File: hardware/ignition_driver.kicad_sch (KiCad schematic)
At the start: 12 parts

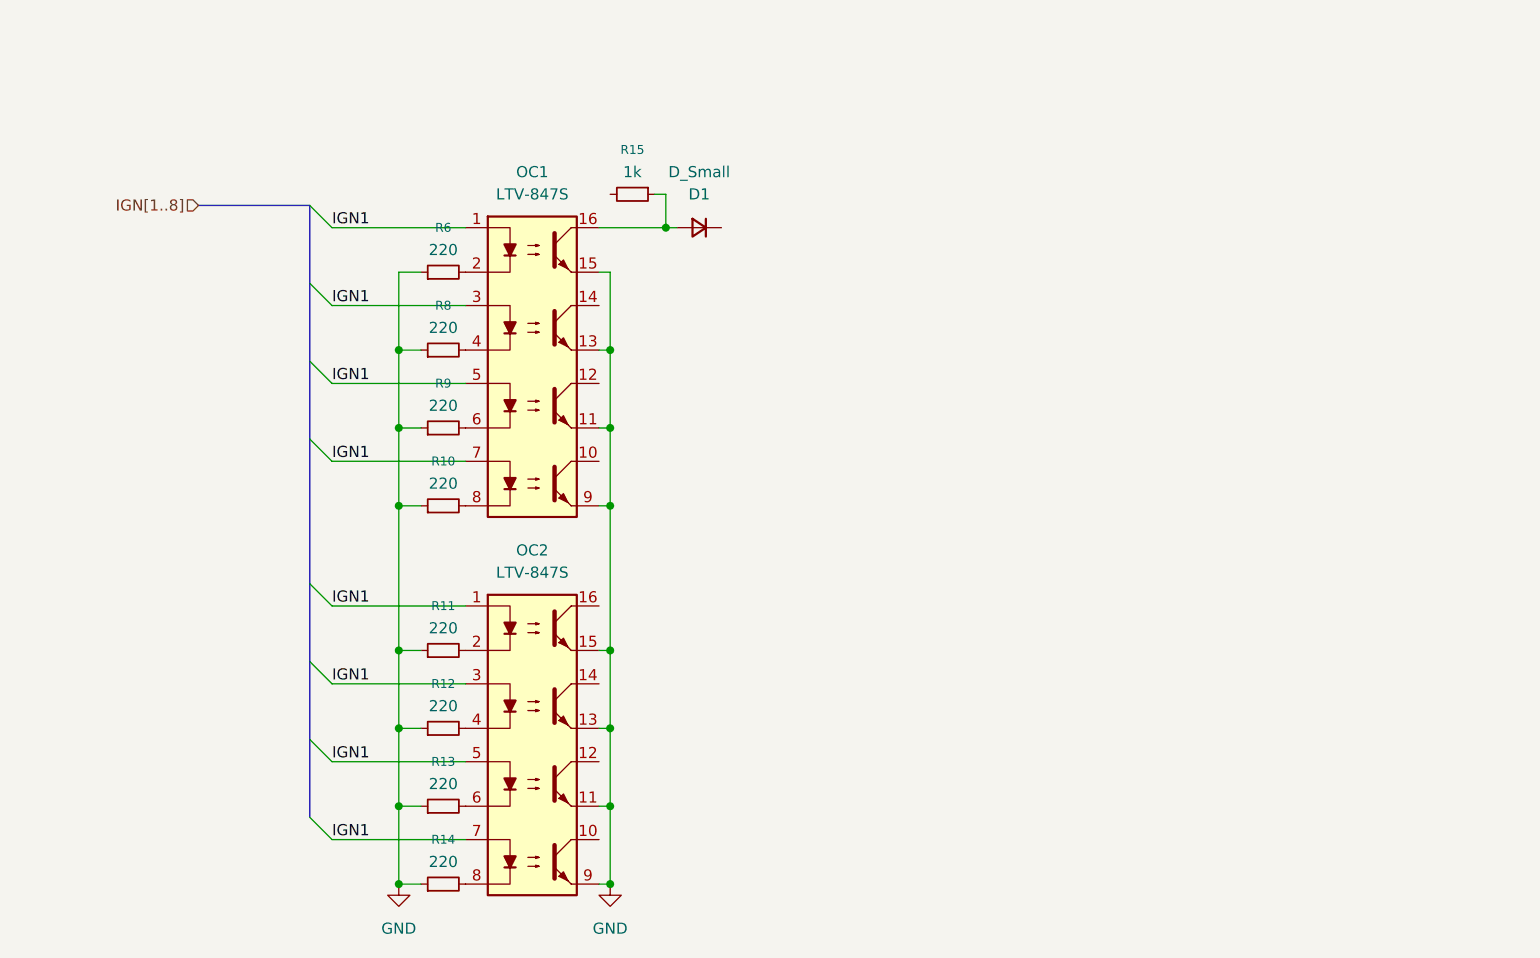
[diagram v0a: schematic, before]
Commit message: Continued IGN driver drawings
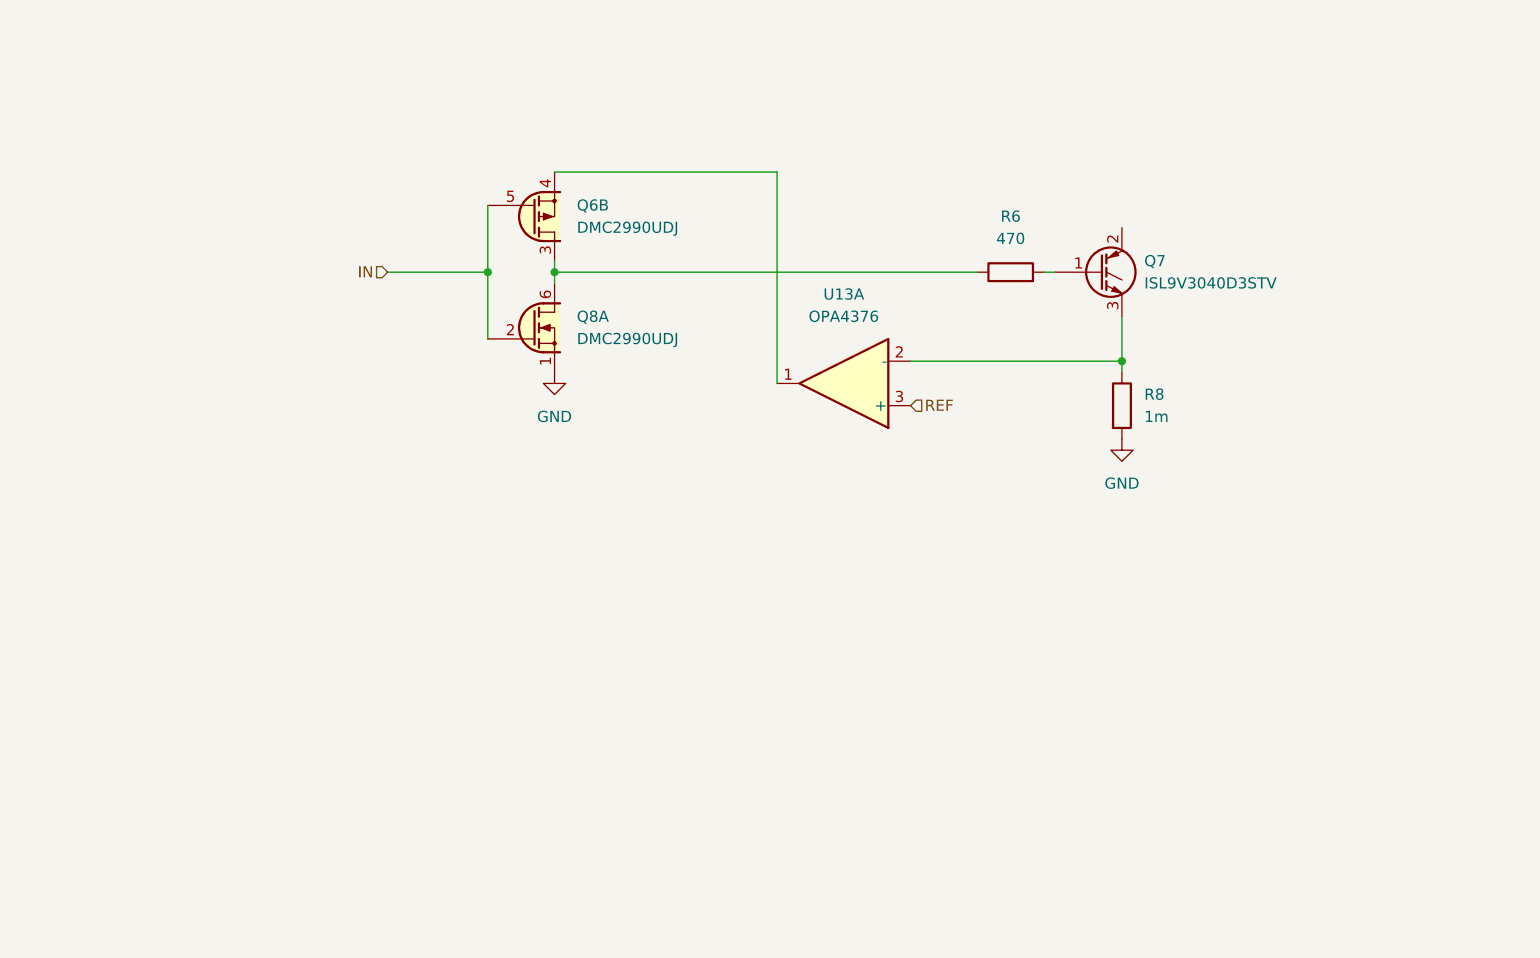
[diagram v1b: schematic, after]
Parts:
- removed D1: D_Small, symbol Device:D_Small
- removed OC1, OC2: LTV-847S, PCM_Package_DIP_AKL:SMDIP-16_W9.53mm, symbol PCM_Optocoupler_AKL:LTV-847S
- removed R10, R11, R12, R13, R14, R6, R8, R9: 220, symbol Device:R_Small
- removed R15: 1k, symbol Device:R_Small
- added Q6, Q8: DMC2990UDJ, PCM_Package_TO_SOT_SMD_AKL:SOT-963, symbol PCM_Transistor_MOSFET_AKL:DMC2990UDJ
- added Q7: ISL9V3040D3STV, Package_TO_SOT_SMD:TO-252-3_TabPin2, symbol Device:Q_NIGBT_GCE
- added R6: 470, symbol Device:R
- added R8: 1m, symbol Device:R
- added U13: OPA4376, symbol Amplifier_Operational:OPA4376
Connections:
- net GND: now also Q8.1 (S1), R8.2
- new net: Q7.1 (G), R6.2
- new net: Q7.3 (E), R8.1, U13.2 (-)
- new net: Q6.4 (S2), U13.1
- new net: Q6.3 (D2), Q8.6 (D1), R6.1
- new net IN: Q6.5 (G2), Q8.2 (G1)
- new net REF: U13.3 (+)

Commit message: Finished preliminary IGN driver
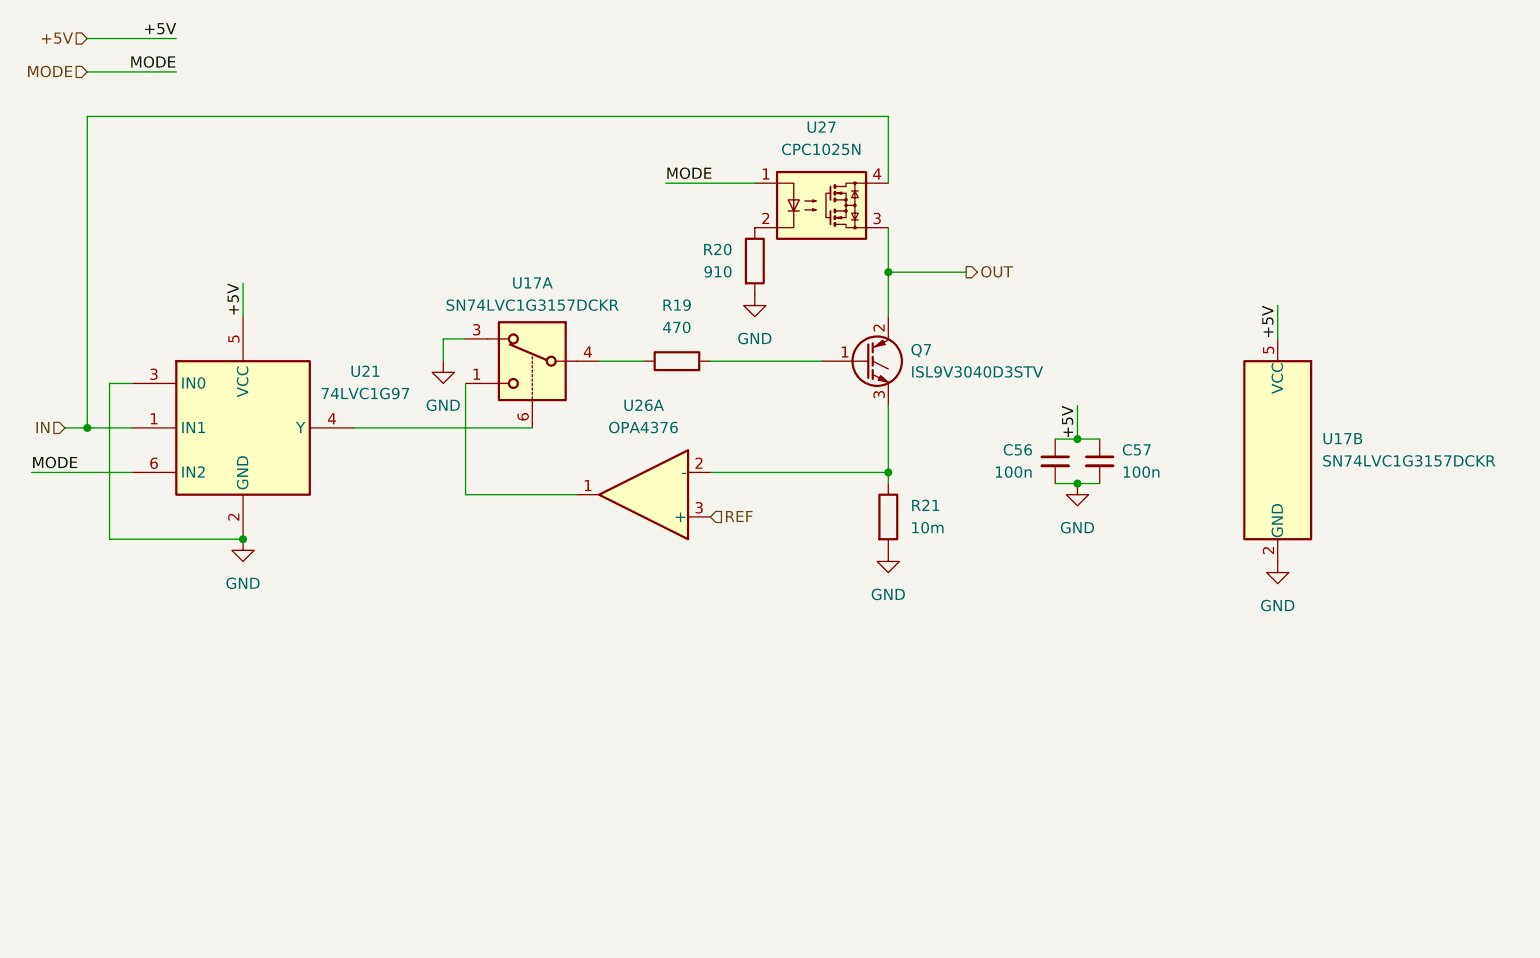
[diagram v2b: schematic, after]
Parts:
- removed Q6, Q8: DMC2990UDJ, PCM_Package_TO_SOT_SMD_AKL:SOT-963, symbol PCM_Transistor_MOSFET_AKL:DMC2990UDJ
- added C56, C57: 100n, symbol Device:C_Small
- added R20: 910, symbol Device:R
- added U17: SN74LVC1G3157DCKR, Package_TO_SOT_SMD:SOT-23-6, symbol openvcu:SN74LVC1G3157DCKR
- added U21: 74LVC1G97, Package_TO_SOT_SMD:SOT-363_SC-70-6, symbol 74xGxx:74LVC1G97
- added U27: CPC1025N, Package_SO:SOP-4_3.8x4.1mm_P2.54mm, symbol Relay_SolidState:CPC1025N
- R21: renamed from R8; value 1m -> 10m
- renumbered R6 to R19, U13 to U26
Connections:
- net GND: now also C56.2, C57.2, R20.2, U17.2 (GND), U17.3, U21.2 (GND), U21.3 (IN0)
- net IN: now also U21.1 (IN1), U27.4
- net OUT: now reaches Q7.2 (C)
- net OUT: now also U27.3
- net at U26.1: now also U17.1
- net at R19.1: now also U17.4
- new net: U17.6, U21.4 (Y)
- new net: R20.1, U27.2
- new net +5V: C56.1, C57.1, U17.5 (VCC), U21.5 (VCC)
- new net MODE: U21.6 (IN2), U27.1
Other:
- moved on the sheet: Q7, R19, R21, U26A

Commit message: Continued work on IGN drivers
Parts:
- removed U26: OPA4376, symbol Amplifier_Operational:OPA4376
- added U13: TSV914, symbol Amplifier_Operational:TSV914
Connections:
- net REF: now also U13.2 (-)
- net at U17.1: now also U13.1
- net at Q7.3 (E), R21.1: now also U13.3 (+)
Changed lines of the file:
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@@
-	)
-	(symbol
-		(lib_id "Amplifier_Operational:OPA4376")
-		(at 92.71 74.93 180)
-		(unit 1)
-		(body_style 1)
-		(exclude_from_sim no)
-		(in_bom yes)
-		(on_board yes)
-		(in_pos_files yes)
-		(dnp no)
-		(fields_autoplaced yes)
-		(property "Reference" "U26"
-			(at 92.71 64.77 0)
-			(show_name no)
-			(do_not_autoplace no)
-			(effects
-				(font
-					(size 1.27 1.27)
-				)
-			)
-		)
-		(property "Value" "OPA4376"
-			(at 92.71 67.31 0)
-			(show_name no)
-			(do_not_autoplace no)
-			(effects
-				(font
-					(size 1.27 1.27)
-				)
-			)
-		)
-		(property "Footprint" ""
-			(at 93.98 77.47 0)
-			(hide yes)
-			(show_name no)
-			(do_not_autoplace no)
-			(effects
-				(font
-					(size 1.27 1.27)
-				)
-			)
-		)
-		(property "Datasheet" "http://www.ti.com/lit/ds/symlink/opa376.pdf"
-			(at 91.44 80.01 0)
-			(hide yes)
-			(show_name no)
-			(do_not_autoplace no)
-			(effects
-				(font
-					(size 1.27 1.27)
-				)
-			)
-		)
-		(property "Description" "Quad Low-Noise, Low Quiescent Current, Precision Operational Amplifier e-trim Series, SC-70-5"
-			(at 92.71 74.93 0)
-			(hide yes)
-			(show_name no)
-			(do_not_autoplace no)
-			(effects
-				(font
-					(size 1.27 1.27)
-				)
-			)
-		)
-		(pin "6"
-		)
-		(pin "5"
-		)
-		(pin "7"
-		)
-		(pin "9"
-		)
-		(pin "14"
-		)
-		(pin "8"
-		)
-		(pin "12"
-		)
-		(pin "1"
-		)
-		(pin "2"
-		)
-		(pin "3"
-		)
-		(pin "10"
-		)
-		(pin "13"
-		)
-		(pin "11"
-		)
-		(pin "4"
-		)
-		(instances
-			(project "openvcu"
-				(path "/474f8017-6a20-4212-a4d1-1038f3d193b2/0e0f3168-a2d1-4cc4-babd-f9e64b91c1ea/6cc00cbf-89c2-4b1d-8fa8-5e3131255cb0"
-					(reference "U26")
-					(unit 1)
-				)
-			)
-		)
 	)
 	(symbol
@@
 					(unit 1)
 				)
+			)
+		)
+	)
+	(symbol
+		(lib_id "Amplifier_Operational:TSV914")
+		(at 92.71 74.93 0)
+		(mirror y)
+		(unit 1)
+		(body_style 1)
+		(exclude_from_sim no)
+		(in_bom yes)
+		(on_board yes)
+		(in_pos_files yes)
+		(dnp no)
+		(property "Reference" "U13"
+			(at 92.71 64.77 0)
+			(show_name no)
+			(do_not_autoplace no)
+			(effects
+				(font
+					(size 1.27 1.27)
+				)
+			)
+		)
+		(property "Value" "TSV914"
+			(at 92.71 67.31 0)
+			(show_name no)
+			(do_not_autoplace no)
+			(effects
+				(font
+					(size 1.27 1.27)
+				)
+			)
+		)
+		(property "Footprint" ""
+			(at 93.98 72.39 0)
+			(hide yes)
+			(show_name no)
+			(do_not_autoplace no)
+			(effects
+				(font
+					(size 1.27 1.27)
+				)
+			)
+		)
+		(property "Datasheet" "www.st.com/resource/en/datasheet/tsv911.pdf"
+			(at 91.44 69.85 0)
+			(hide yes)
+			(show_name no)
+			(do_not_autoplace no)
+			(effects
+				(font
+					(size 1.27 1.27)
+				)
+			)
+		)
+		(property "Description" "Quad rail-to-rail input/output 8 MHz operational amplifiers, SOIC-14/TSSOP-14"
+			(at 92.71 74.93 0)
+			(hide yes)
+			(show_name no)
+			(do_not_autoplace no)
+			(effects
+				(font
+					(size 1.27 1.27)
+				)
+			)
+		)
+		(pin "7"
+		)
+		(pin "13"
+		)
+		(pin "9"
+		)
+		(pin "12"
+		)
+		(pin "3"
+		)
+		(pin "6"
+		)
+		(pin "5"
+		)
+		(pin "10"
+		)
+		(pin "1"
+		)
+		(pin "2"
+		)
+		(pin "8"
+		)
+		(pin "4"
+		)
+		(pin "11"
+		)
+		(pin "14"
+		)
+		(instances
+			(project "openvcu"
+				(path "/474f8017-6a20-4212-a4d1-1038f3d193b2/0e0f3168-a2d1-4cc4-babd-f9e64b91c1ea/6cc00cbf-89c2-4b1d-8fa8-5e3131255cb0"
+					(reference "U13")
+					(unit 1)
+				)

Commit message: Need to revisit current limitation (use PWM), need to use charge pump for CCM of output drivers
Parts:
- removed Q7: ISL9V3040D3STV, Package_TO_SOT_SMD:TO-252-3_TabPin2, symbol Device:Q_NIGBT_GCE
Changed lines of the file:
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@@
-	)
-	(symbol
-		(lib_id "Device:Q_NIGBT_GCE")
-		(at 118.11 59.69 0)
-		(unit 1)
-		(body_style 1)
-		(exclude_from_sim no)
-		(in_bom yes)
-		(on_board yes)
-		(in_pos_files yes)
-		(dnp no)
-		(fields_autoplaced yes)
-		(property "Reference" "Q7"
-			(at 123.19 58.4199 0)
-			(show_name no)
-			(do_not_autoplace no)
-			(effects
-				(font
-					(size 1.27 1.27)
-				)
-				(justify left)
-			)
-		)
-		(property "Value" "ISL9V3040D3STV"
-			(at 123.19 60.9599 0)
-			(show_name no)
-			(do_not_autoplace no)
-			(effects
-				(font
-					(size 1.27 1.27)
-				)
-				(justify left)
-			)
-		)
-		(property "Footprint" "Package_TO_SOT_SMD:TO-252-3_TabPin2"
-			(at 123.19 57.15 0)
-			(hide yes)
-			(show_name no)
-			(do_not_autoplace no)
-			(effects
-				(font
-					(size 1.27 1.27)
-				)
-			)
-		)
-		(property "Datasheet" "https://www.onsemi.com/pdf/datasheet/isl9v3040d3stv-d.pdf"
-			(at 118.11 59.69 0)
-			(hide yes)
-			(show_name no)
-			(do_not_autoplace no)
-			(effects
-				(font
-					(size 1.27 1.27)
-				)
-			)
-		)
-		(property "Description" "N-IGBT transistor, gate/collector/emitter"
-			(at 118.11 59.69 0)
-			(hide yes)
-			(show_name no)
-			(do_not_autoplace no)
-			(effects
-				(font
-					(size 1.27 1.27)
-				)
-			)
-		)
-		(pin "1"
-		)
-		(pin "3"
-		)
-		(pin "2"
-		)
-		(instances
-			(project "openvcu"
-				(path "/474f8017-6a20-4212-a4d1-1038f3d193b2/0e0f3168-a2d1-4cc4-babd-f9e64b91c1ea/6cc00cbf-89c2-4b1d-8fa8-5e3131255cb0"
-					(reference "Q7")
-					(unit 1)
-				)
-			)
-		)
 	)
 	(symbol
